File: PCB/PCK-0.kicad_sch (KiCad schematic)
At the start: 93 parts, among them J1 USB_C_Receptacle_USB2.0_16P, J2 BAT+, J3 BAT-, J4 Conn_01x15, SW1 EN, SW10 1,2, SW11 2,2, SW12 3,2, SW13 4,2, SW14 5,2, SW15 6,2, SW16 1,3, SW17 2,3, SW18 3,3, SW19 4,3, SW2 BOOT, SW20 5,3, SW21 6,3, SW22 1,4, SW23 2,4, SW24 3,4, SW25 4,4, SW26 5,4, SW27 6,4, SW28 1,4, SW29 2,4, SW3 RotaryEncoder_Switch_MP, SW30 3,4, SW31 4,4, SW32 5,4, SW33 6,4, SW4 1,1, SW5 2,1, SW6 3,1, SW7 4,1, SW8 5,1, SW9 6,1, U1 NCP1117-3.3_SOT223, U2 NCP1117-3.3_SOT223, U3 USBLC6-2SC6, U4 ESP32-C6-MINI-1, U5 TVS1400DRV

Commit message: double sided probably works
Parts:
- added J5: Conn_01x15_Socket, symbol Connector:Conn_01x15_Socket
- D10, D11, D12, D13, D14, D15, D16, D17, D18, D19, D20, D21, D22, D23, D24, D25, D26, D27, D28, D29, D3, D30, D31, D32, D4, D5, D6, D7, D8, D9: footprint Diode_SMD:D_0805_2012Metric -> Diode_THT:D_A-405_P2.54mm_Vertical_AnodeUp
- SW10, SW11, SW12, SW13, SW14, SW15, SW16, SW17, SW18, SW19, SW20, SW21, SW22, SW23, SW24, SW25, SW26, SW27, SW28, SW29, SW30, SW31, SW32, SW33, SW4, SW5, SW6, SW7, SW8, SW9: footprint kb_switch:Kailh_socket_MX_reversible -> KB_SWITCH:SW_MX_reversible

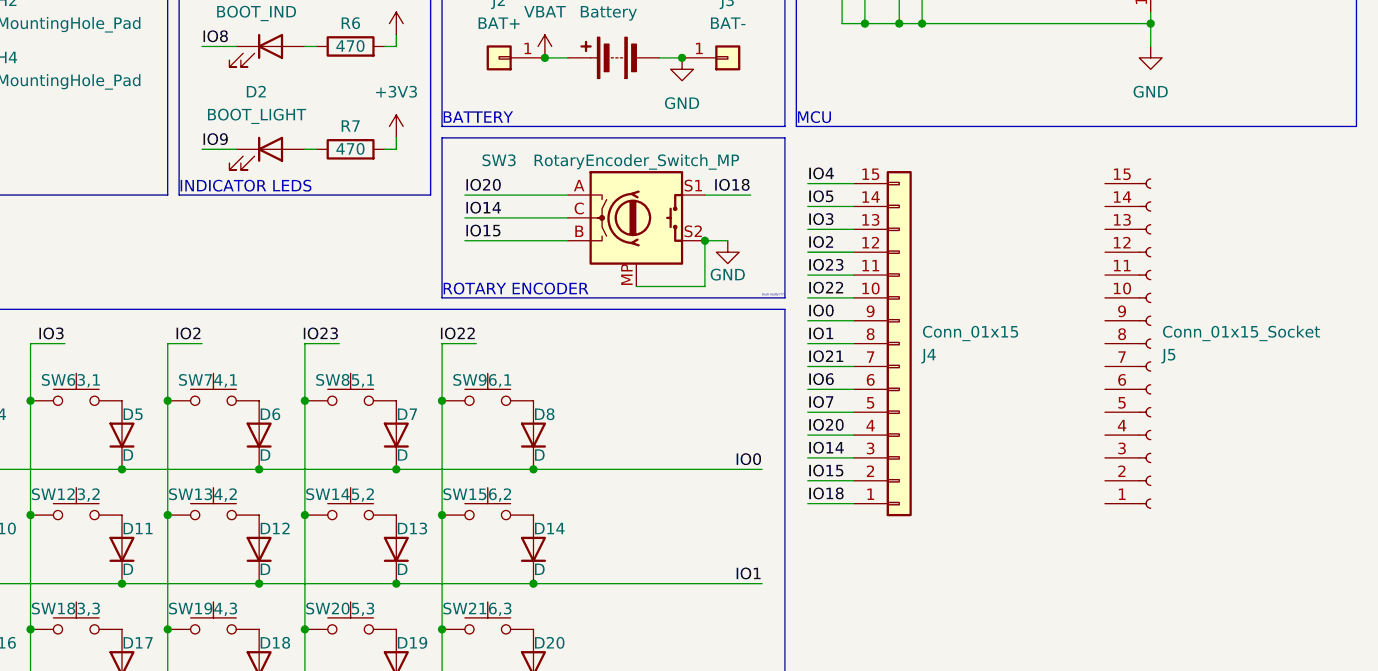
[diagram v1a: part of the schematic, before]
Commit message: diode changed to SMD, mounting holes
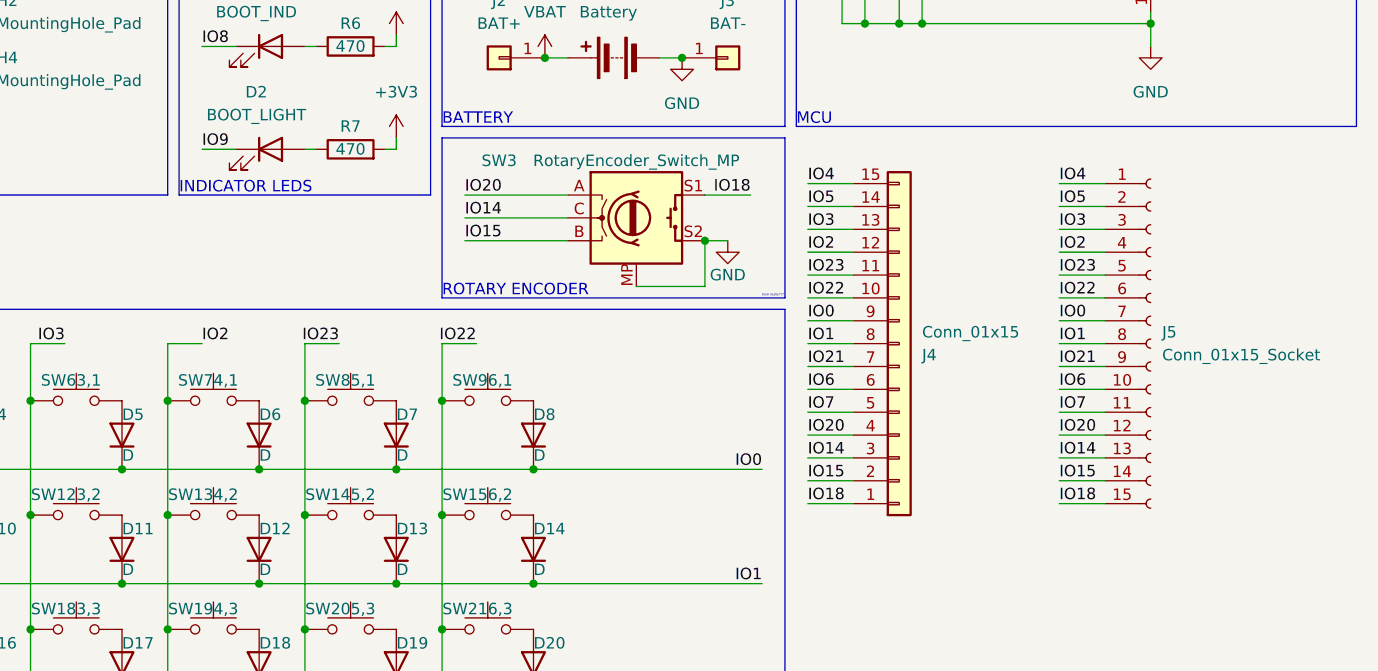
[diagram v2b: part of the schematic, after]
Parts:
- D10, D11, D12, D13, D14, D15, D16, D17, D18, D19, D20, D21, D22, D23, D24, D25, D26, D27, D28, D29, D3, D30, D31, D32, D4, D5, D6, D7, D8, D9: footprint Diode_THT:D_A-405_P2.54mm_Vertical_AnodeUp -> Diode_SMD:D_0805_2012Metric
- H1, H2, H3, H4: footprint MountingHole:MountingHole_3.2mm_M3_Pad -> MountingHole:MountingHole_3.2mm_M3
- J5: footprint (none) -> Connector_PinSocket_1.00mm:PinSocket_1x15_P1.00mm_Vertical
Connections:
- net IO0: now also J5.7 (Pin_7)
- net IO1: now also J5.8 (Pin_8)
- net IO14: now also J5.13 (Pin_13)
- net IO15: now also J5.14 (Pin_14)
- net IO18: now also J5.15 (Pin_15)
- net IO2: now also J5.4 (Pin_4)
- net IO20: now also J5.12 (Pin_12)
- net IO21: now also J5.9 (Pin_9)
- net IO22: now also J5.6 (Pin_6)
- net IO23: now also J5.5 (Pin_5)
- net IO3: now also J5.3 (Pin_3)
- net IO4: now also J5.1 (Pin_1)
- net IO5: now also J5.2 (Pin_2)
- net IO6: now also J5.10 (Pin_10)
- net IO7: now also J5.11 (Pin_11)
